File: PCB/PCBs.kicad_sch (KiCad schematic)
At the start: 56 parts, among them CN1 W2A41C681KAT2A, CN5 W2A41C681KAT2A, CN6 W2A41C681KAT2A, CN7 W2A41C681KAT2A, U1 ADS1299IPAGR, U10 TPD4E1B06DCKR, U11 TPS61023DRLR, U3 TPD4E1B06DCKR, U4 TPD4E1B06DCKR, U5 TPS73225DBVR, U7 LM2664M6, U8 TPS73233DBVT, U9 TPS72325DBVT

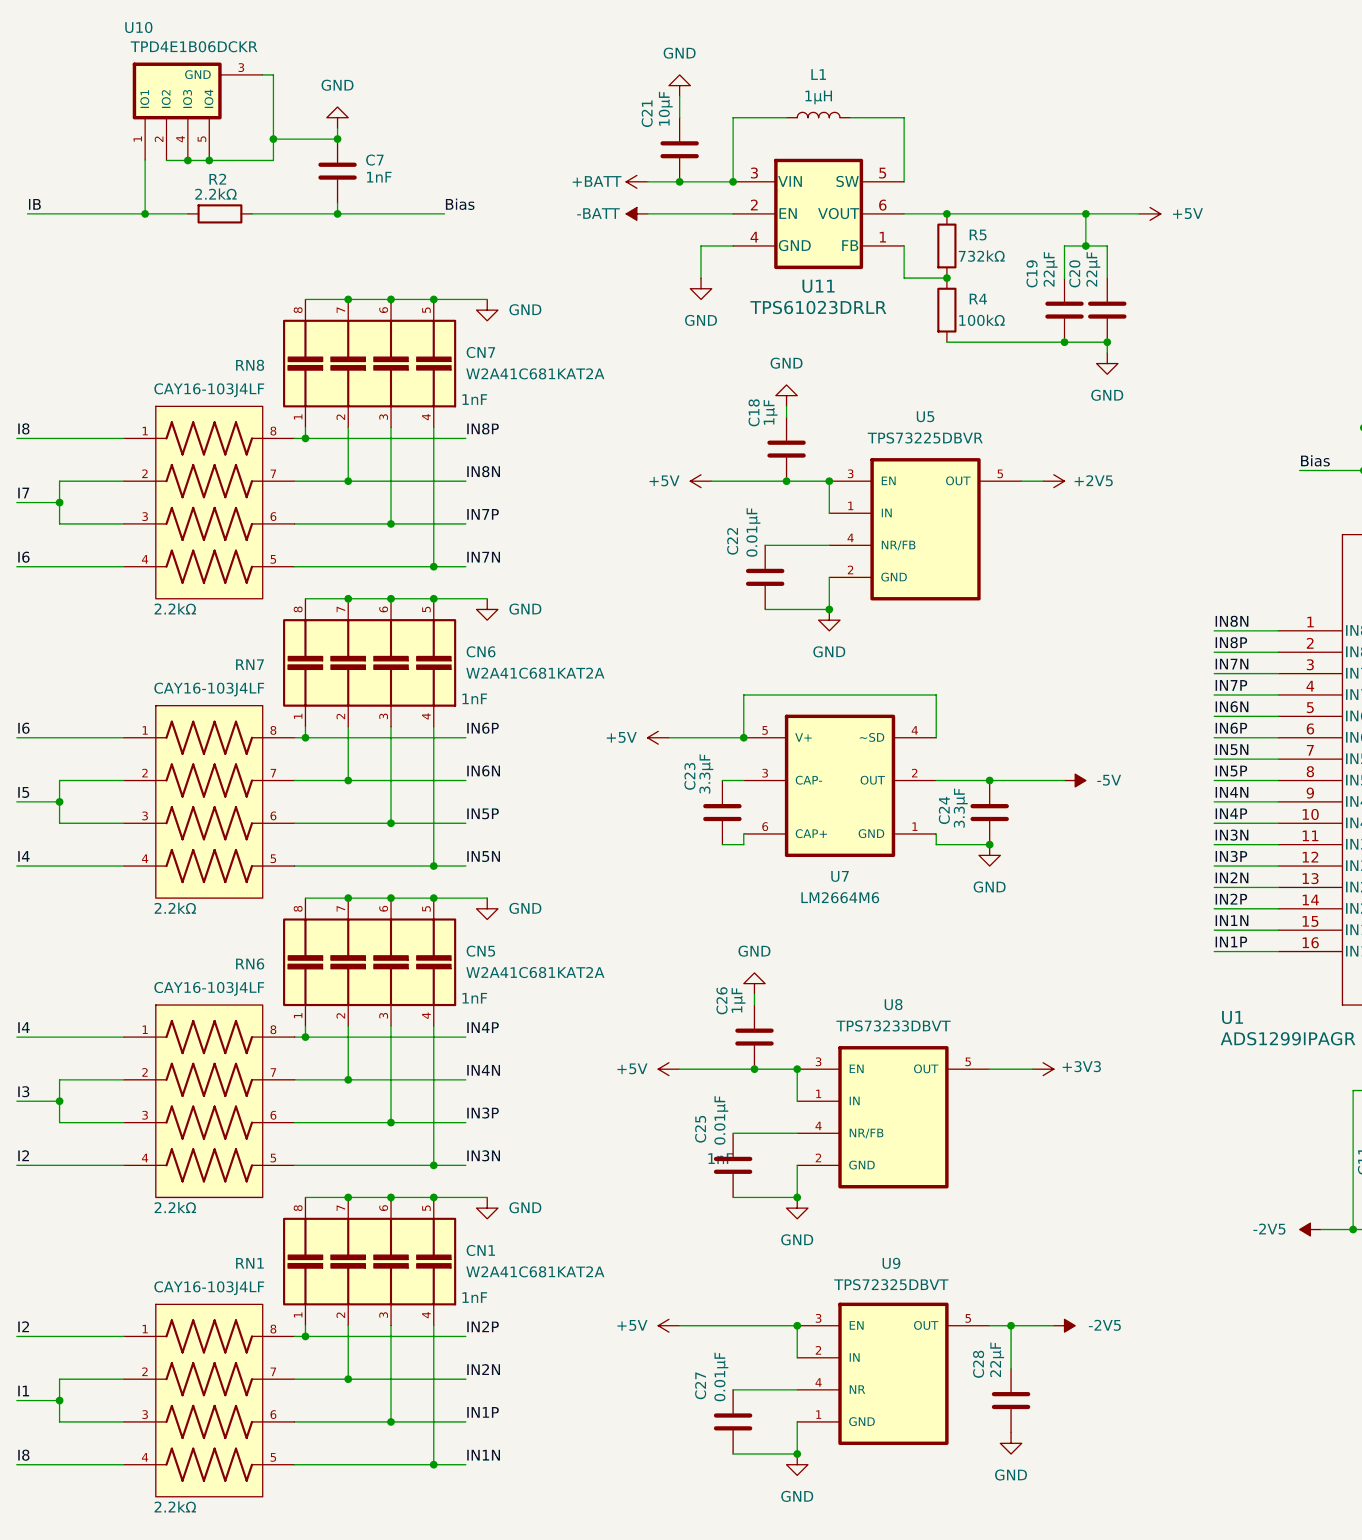
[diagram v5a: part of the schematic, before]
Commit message: power on own sheet
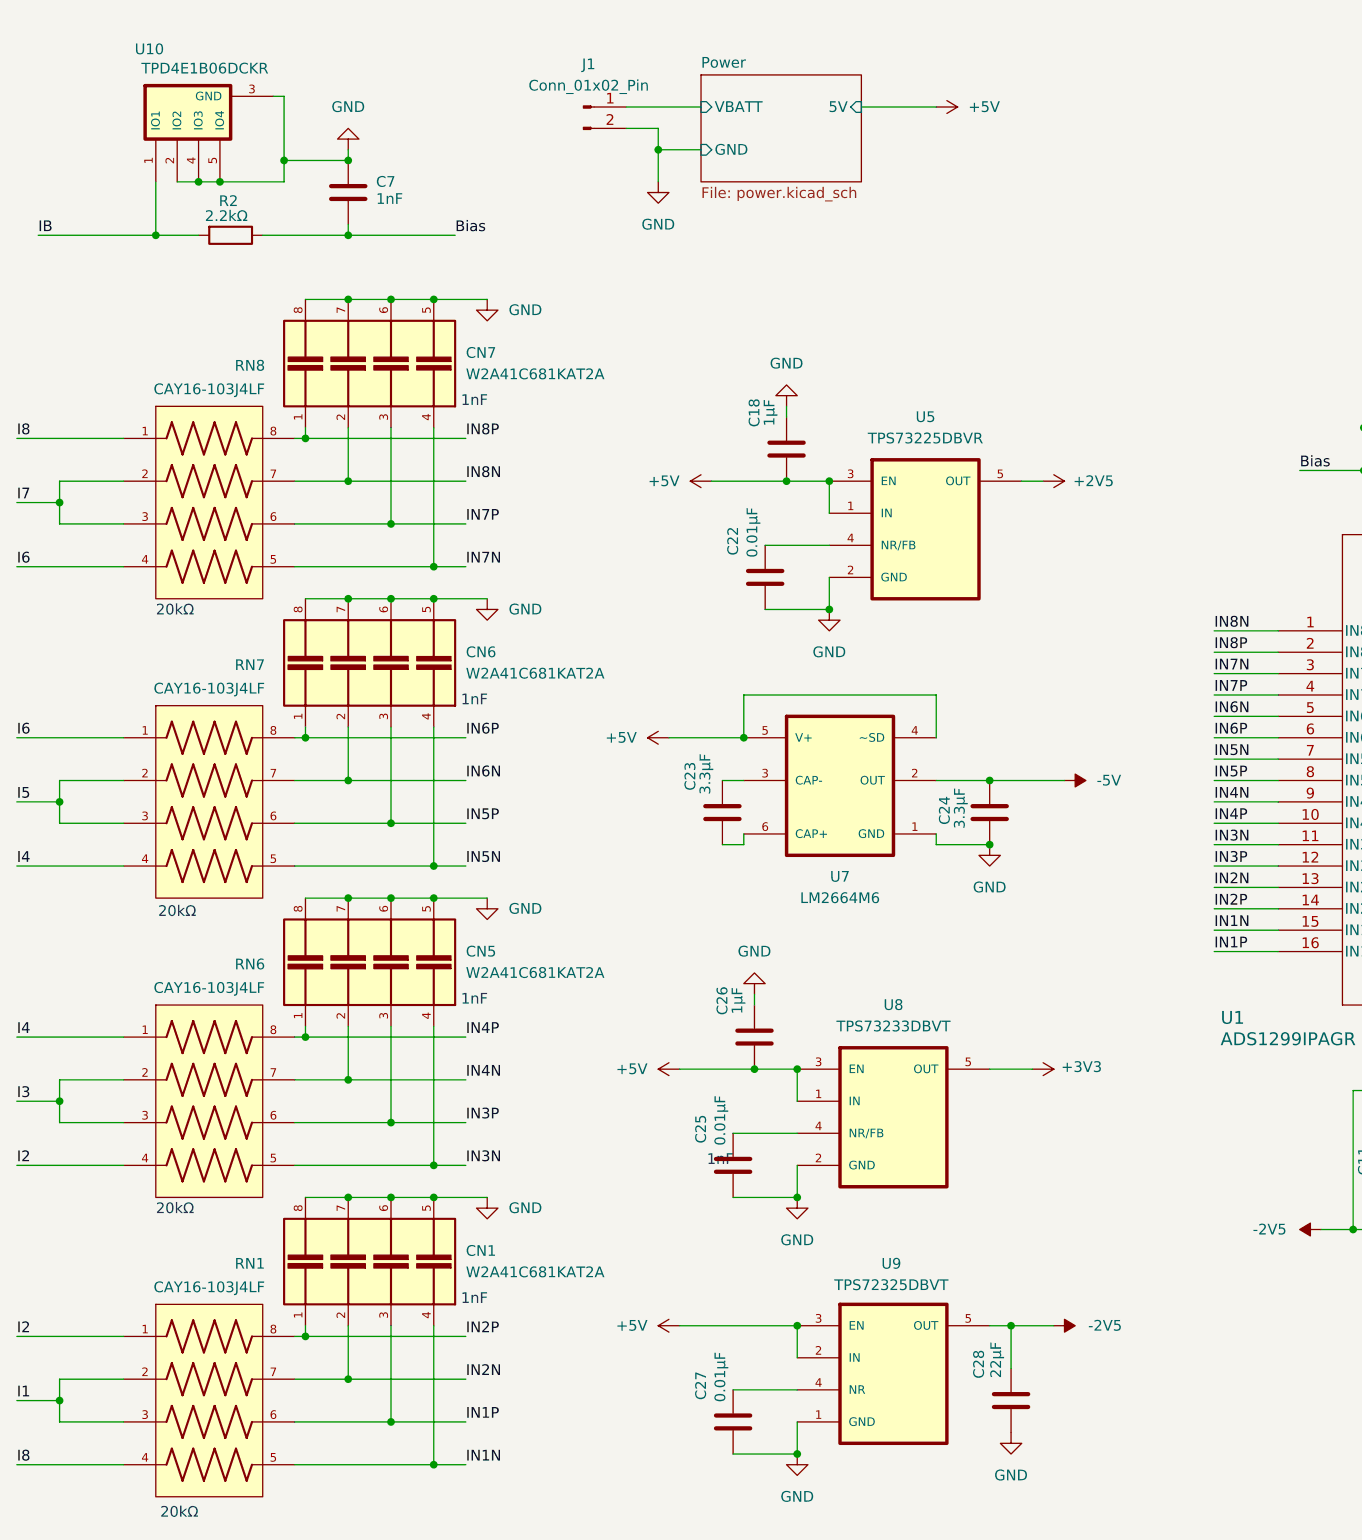
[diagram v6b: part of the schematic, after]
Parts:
- removed C19, C20: 22µF, symbol Device:C
- removed C21: 10µF, symbol Device:C
- removed L1: 1µH, symbol Device:L
- removed R4: 100kΩ, symbol Device:R
- removed R5: 732kΩ, symbol Device:R
- removed U11: TPS61023DRLR, DRL0006A, symbol custom_lib:TPS61023DRLR
- added J1: Conn_01x02_Pin, symbol Connector:Conn_01x02_Pin
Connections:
- net GND: now also J1.2 (Pin_2)
- new net Power/VBATT: J1.1 (Pin_1)
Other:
- added sheet Power (power.kicad_sch)
- note added: "20kΩ"
- note removed: "2.2kΩ"
- moved on the sheet: C7, R2, U10

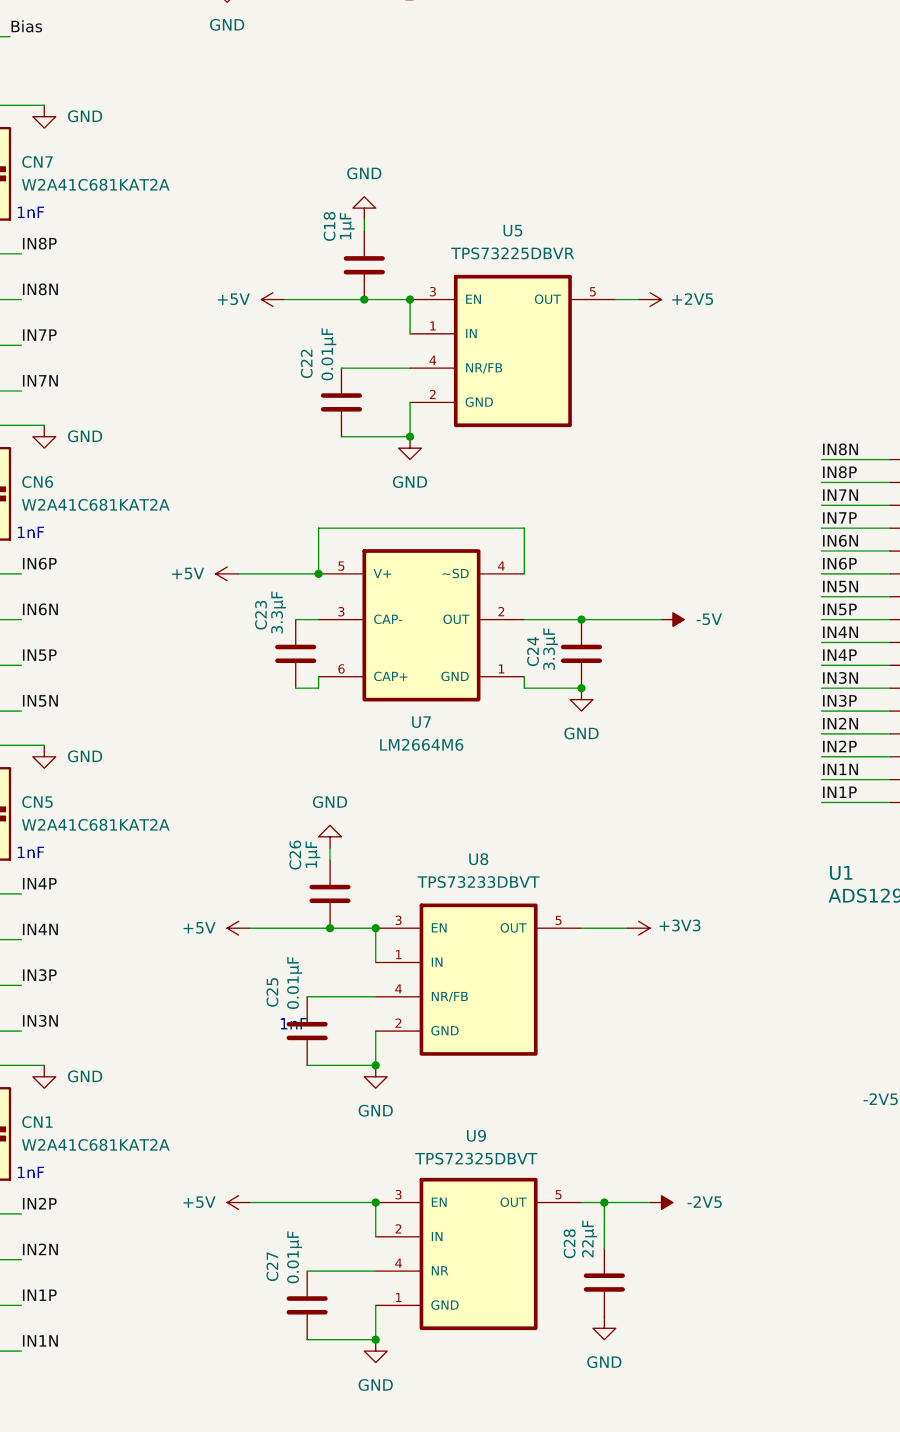
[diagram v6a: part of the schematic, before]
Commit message: volt reg to power page
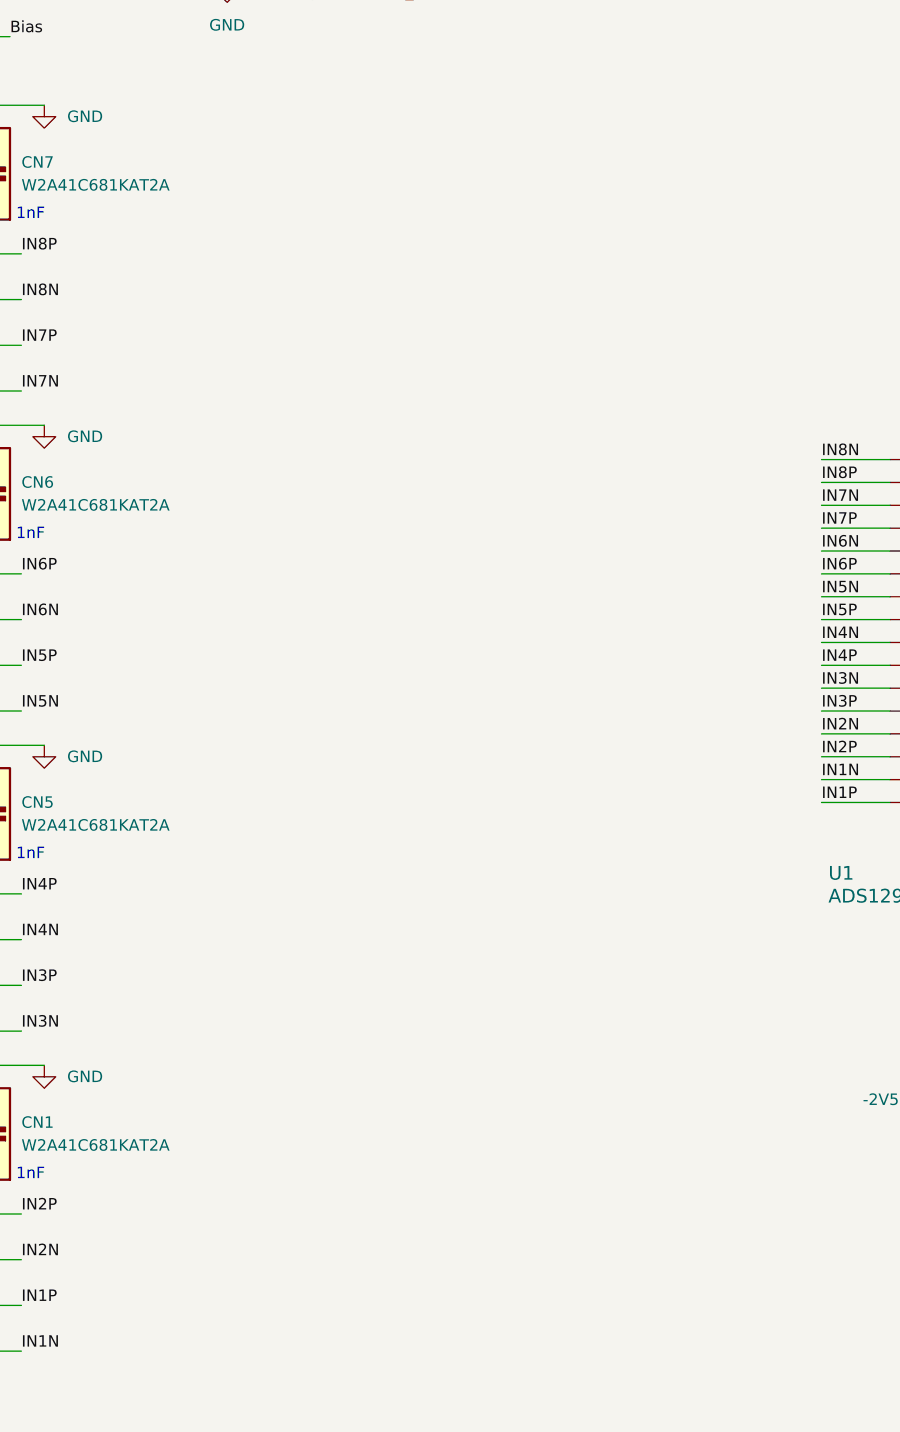
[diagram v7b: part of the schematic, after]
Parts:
- removed C18, C26: 1µF, symbol Device:C
- removed C22, C25, C27: 0.01µF, symbol Device:C
- removed C23, C24: 3.3µF, symbol Device:C
- removed C28: 22µF, symbol Device:C
- removed U5: TPS73225DBVR, TPS73225DBVR:SOT95P280X145-5N, symbol custom_lib:TPS73225DBVR
- removed U7: LM2664M6, LM2664M6:SOT95P300X120-6N, symbol custom_lib:LM2664M6
- removed U8: TPS73233DBVT, TPS73233DBVT:SOT95P280X145-5N, symbol custom_lib:TPS73233DBVT
- removed U9: TPS72325DBVT, TPS72325DBVT:SOT95P280X145-5N, symbol custom_lib:TPS72325DBVT

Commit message: other pages for volt regs
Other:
- sheet Power renamed Booster
- added sheet 5Vto-2V5 (5Vto-2V5.kicad_sch)
- added sheet 5Vto-5V (5Vto-5V.kicad_sch)
- added sheet 5Vto2V5 (5Vto2V5.kicad_sch)
- added sheet 5Vto3V3 (5Vto3V3.kicad_sch)
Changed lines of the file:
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@@
 	)
 	(junction
-		(at 95.25 29.21)
+		(at 224.79 60.96)
 		(diameter 0)
 		(color 0 0 0 0)
 	)
 	(junction
-		(at 224.79 60.96)
+		(at 68.58 78.74)
 		(diameter 0)
 		(color 0 0 0 0)
 	)
 	(junction
-		(at 68.58 78.74)
+		(at 68.58 46.99)
 		(diameter 0)
 		(color 0 0 0 0)
 	)
 	(junction
-		(at 68.58 46.99)
+		(at 95.25 29.21)
 		(diameter 0)
 		(color 0 0 0 0)
@@
 	(wire
 		(pts
+			(xy 95.25 29.21) (xy 95.25 33.02)
+		)
+		(stroke
+			(width 0)
+			(type default)
+		)
+	)
+	(wire
+		(pts
 			(xy 53.34 170.18) (xy 53.34 168.91)
 		)
@@
 	(wire
 		(pts
-			(xy 119.38 24.13) (xy 128.27 24.13)
+			(xy 115.57 24.13) (xy 124.46 24.13)
 		)
 		(stroke
@@
 	(wire
 		(pts
-			(xy 95.25 29.21) (xy 95.25 26.67)
-		)
-		(stroke
-			(width 0)
-			(type default)
-		)
-	)
-	(wire
-		(pts
 			(xy 240.03 132.08) (xy 242.57 132.08)
 		)
@@
 	(wire
 		(pts
-			(xy 95.25 33.02) (xy 95.25 29.21)
-		)
-		(stroke
-			(width 0)
-			(type default)
-		)
-	)
-	(wire
-		(pts
 			(xy 19.05 177.8) (xy 24.13 177.8)
 		)
@@
 	(wire
 		(pts
+			(xy 95.25 26.67) (xy 95.25 29.21)
+		)
+		(stroke
+			(width 0)
+			(type default)
+		)
+	)
+	(wire
+		(pts
 			(xy 200.66 157.48) (xy 205.74 157.48)
 		)
@@
 	(symbol
 		(lib_id "power:+5V")
-		(at 128.27 24.13 270)
+		(at 124.46 24.13 270)
 		(unit 1)
 		(exclude_from_sim no)
@@
 		(fields_autoplaced yes)
 		(property "Reference" "#PWR015"
-			(at 124.46 24.13 0)
+			(at 120.65 24.13 0)
 			(effects
 				(font
@@
 		)
 		(property "Value" "+5V"
-			(at 132.08 24.1299 90)
+			(at 128.27 24.1299 90)
 			(effects
 				(font
@@
 		)
 		(property "Footprint" ""
-			(at 128.27 24.13 0)
+			(at 124.46 24.13 0)
 			(effects
 				(font
@@
 		)
 		(property "Datasheet" ""
-			(at 128.27 24.13 0)
+			(at 124.46 24.13 0)
 			(effects
 				(font
@@
 		)
 		(property "Description" "Power symbol creates a global label with name \"+5V\""
-			(at 128.27 24.13 0)
+			(at 124.46 24.13 0)
 			(effects
 				(font
@@
 	)
 	(sheet
+		(at 100.33 106.68)
+		(size 15.24 12.7)
+		(fields_autoplaced yes)
+		(stroke
+			(width 0.1524)
+			(type solid)
+		)
+		(fill
+			(color 0 0 0 0.0000)
+		)
+		(property "Sheetname" "5Vto2V5"
+			(at 100.33 105.9684 0)
+			(effects
+				(font
+					(size 1.27 1.27)
+				)
+				(justify left bottom)
+			)
+		)
+		(property "Sheetfile" "5Vto2V5.kicad_sch"
+			(at 100.33 119.9646 0)
+			(effects
+				(font
+					(size 1.27 1.27)
+				)
+				(justify left top)
+			)
+		)
+		(instances
+			(project "PCBs"
+				(path "/5beccadf-d27e-4f5e-8faf-404ef06d8def"
+					(page "6")
+				)
+			)
+		)
+	)
+	(sheet
+		(at 100.33 67.31)
+		(size 15.24 12.7)
+		(fields_autoplaced yes)
+		(stroke
+			(width 0.1524)
+			(type solid)
+		)
+		(fill
+			(color 0 0 0 0.0000)
+		)
+		(property "Sheetname" "5Vto-2V5"
+			(at 100.33 66.5984 0)
+			(effects
+				(font
+					(size 1.27 1.27)
+				)
+				(justify left bottom)
+			)
+		)
+		(property "Sheetfile" "5Vto-2V5.kicad_sch"
+			(at 100.33 80.5946 0)
+			(effects
+				(font
+					(size 1.27 1.27)
+				)
+				(justify left top)
+			)
+		)
+		(instances
+			(project "PCBs"
+				(path "/5beccadf-d27e-4f5e-8faf-404ef06d8def"
+					(page "4")
+				)
+			)
+		)
+	)
+	(sheet
 		(at 100.33 20.32)
-		(size 19.05 12.7)
+		(size 15.24 12.7)
 		(fields_autoplaced yes)
 		(stroke
@@
 			(color 0 0 0 0.0000)
 		)
-		(property "Sheetname" "Power"
+		(property "Sheetname" "Booster"
 			(at 100.33 19.6084 0)
 			(effects
@@
 		)
 		(pin "5V" input
-			(at 119.38 24.13 0)
+			(at 115.57 24.13 0)
 			(effects
 				(font
@@
 				)
 			)
+		)
+	)
+	(sheet
+		(at 100.33 46.99)
+		(size 15.24 12.7)
+		(fields_autoplaced yes)
+		(stroke
+			(width 0.1524)
+			(type solid)
+		)
+		(fill
+			(color 0 0 0 0.0000)
+		)
+		(property "Sheetname" "5Vto-5V"
+			(at 100.33 46.2784 0)
+			(effects
+				(font
+					(size 1.27 1.27)
+				)
+				(justify left bottom)
+			)
+		)
+		(property "Sheetfile" "5Vto-5V.kicad_sch"
+			(at 100.33 60.2746 0)
+			(effects
+				(font
+					(size 1.27 1.27)
+				)
+				(justify left top)
+			)
+		)
+		(pin "5V" input
+			(at 100.33 50.8 180)
+			(effects
+				(font
+					(size 1.27 1.27)
+				)
+				(justify left)
+			)
+		)
+		(pin "GND" input
+			(at 100.33 55.88 180)
+			(effects
+				(font
+					(size 1.27 1.27)
+				)
+				(justify left)
+			)
+		)
+		(pin "-5V" output
+			(at 115.57 50.8 0)
+			(effects
+				(font
+					(size 1.27 1.27)
+				)
+				(justify right)
+			)
+		)
+		(instances
+			(project "PCBs"
+				(path "/5beccadf-d27e-4f5e-8faf-404ef06d8def"
+					(page "3")
+				)
+			)
+		)
+	)
+	(sheet
+		(at 100.33 86.36)
+		(size 15.24 12.7)
+		(fields_autoplaced yes)
+		(stroke
+			(width 0.1524)
+			(type solid)
+		)
+		(fill
+			(color 0 0 0 0.0000)
+		)
+		(property "Sheetname" "5Vto3V3"
+			(at 100.33 85.6484 0)
+			(effects
+				(font
+					(size 1.27 1.27)
+				)
+				(justify left bottom)
+			)
+		)
+		(property "Sheetfile" "5Vto3V3.kicad_sch"
+			(at 100.33 99.6446 0)
+			(effects
+				(font
+					(size 1.27 1.27)
+				)
+				(justify left top)
+			)
+		)
+		(instances
+			(project "PCBs"
+				(path "/5beccadf-d27e-4f5e-8faf-404ef06d8def"
+					(page "5")
+				)
+			)
